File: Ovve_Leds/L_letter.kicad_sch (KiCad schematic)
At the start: 0 parts

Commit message: Finished preliminary schematics
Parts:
- added D23, D24, D25, D26, D27, D28, D29: LED, symbol Device:LED
- added H19, H20, H21, H22: MountingHole, symbol Mechanical:MountingHole
- added R23, R24, R25, R26, R27, R28, R29: 150, symbol Device:R
- added U3: 74LS174, symbol 74xx:74LS174
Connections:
- net CLK_in_L: now also U3.9 (Cp)
- net DATA_in_L: now also U3.3 (D0)
- new net: D27.2 (A), R27.2
- new net: D28.2 (A), R28.2
- new net: D26.2 (A), R26.2
- new net: D29.2 (A), R29.2
- new net: D24.2 (A), R24.2
- new net: D25.2 (A), R25.2
- new net: D23.2 (A), R23.2
- new net +5V: U3.1 (~{Mr}), U3.16 (VCC)
- new net GND: D23.1 (K), D24.1 (K), D25.1 (K), D26.1 (K), D27.1 (K), D28.1 (K), D29.1 (K), U3.8 (GND)
- new net LED1: R23.1, U3.2 (Q0), U3.4 (D1)
- new net LED2: R24.1, U3.5 (Q1), U3.6 (D2)
- new net LED3: R25.1, U3.11 (D3), U3.7 (Q2)
- new net LED4: R26.1, U3.10 (Q3), U3.13 (D4)
- new net LED5: R27.1, R28.1, R29.1, U3.12 (Q4)
- no-connect marks 0 -> 2

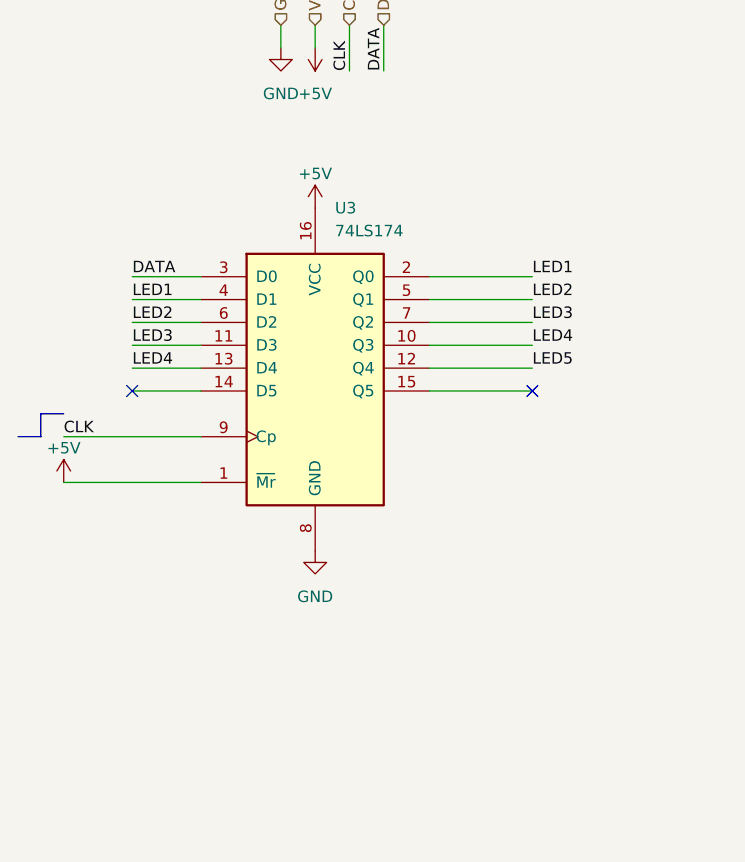
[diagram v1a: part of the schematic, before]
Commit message: Added decoupling capacitors and assigned footprints
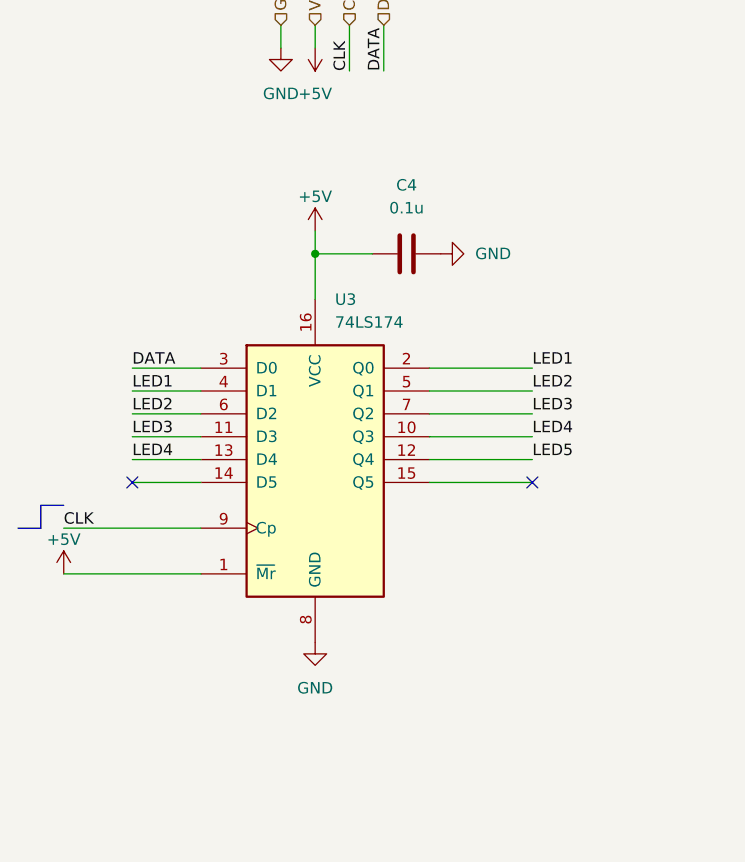
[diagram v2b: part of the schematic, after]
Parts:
- added C4: 0.1u, Capacitor_SMD:C_0603_1608Metric, symbol Device:C
- D23, D24, D25, D26, D27, D28, D29: footprint (none) -> LED_THT:LED_D5.0mm
- H19, H20, H21, H22: footprint (none) -> MountingHole:MountingHole_5.3mm_M5_DIN965_Pad
- R23, R24, R25, R26, R27, R28, R29: footprint (none) -> Resistor_SMD:R_0603_1608Metric
- U3: footprint (none) -> Package_DIP:DIP-16_W7.62mm
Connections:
- net +5V: now also C4.1
- net GND: now also C4.2
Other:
- moved on the sheet: U3

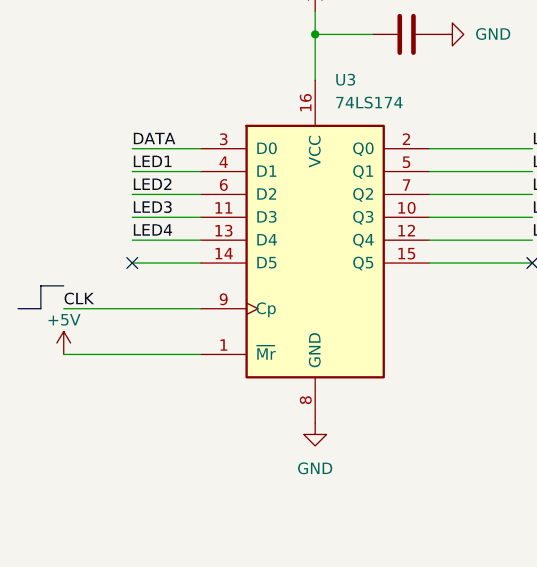
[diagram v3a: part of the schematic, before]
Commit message: Updated flip-flops
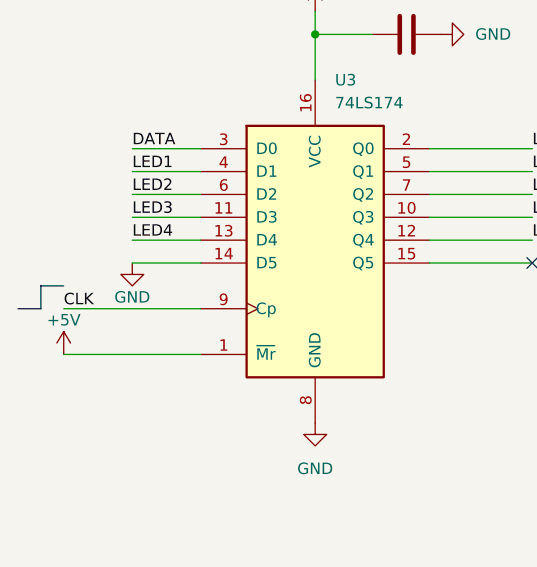
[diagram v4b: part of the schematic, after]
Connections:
- net GND: now also U3.14 (D5)
- no-connect marks 2 -> 1
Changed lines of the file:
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@@
 		(at 74.93 82.55)
-	)
-	(no_connect
-		(at 30.48 82.55)
 	)
 	(wire
@@
 					(unit 1)
 				)
+			)
+		)
+	)
+	(symbol
+		(lib_id "power:GND")
+		(at 30.48 82.55 0)
+		(unit 1)
+		(exclude_from_sim no)
+		(in_bom yes)
+		(on_board yes)
+		(dnp no)
+		(property "Reference" "#PWR074"
+			(at 30.48 88.9 0)
+			(effects
+				(font
+					(size 1.27 1.27)
+				)
+				(hide yes)
+			)
+		)
+		(property "Value" "GND"
+			(at 30.48 86.36 0)
+			(effects
+				(font
+					(size 1.27 1.27)
+				)
+			)
+		)
+		(property "Footprint" ""
+			(at 30.48 82.55 0)
+			(effects
+				(font
+					(size 1.27 1.27)
+				)
+				(hide yes)
+			)
+		)
+		(property "Datasheet" ""
+			(at 30.48 82.55 0)
+			(effects
+				(font
+					(size 1.27 1.27)
+				)
+				(hide yes)
+			)
+		)
+		(property "Description" "Power symbol creates a global label with name \"GND\" , ground"
+			(at 30.48 82.55 0)
+			(effects
+				(font
+					(size 1.27 1.27)
+				)
+				(hide yes)
+			)
+		)
+		(pin "1"
+		)
+		(instances
+			(project "Ovve_Leds"
+				(path "/a3f154e4-ded7-4c3a-b779-1e1dc74aad12/74d7af5f-3f5b-4383-b213-68bb9c4ec1cd"
+					(reference "#PWR074")
+					(unit 1)
+				)

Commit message: Component layout on PCB
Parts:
- removed H21, H22: MountingHole, MountingHole:MountingHole_5.3mm_M5_DIN965_Pad, symbol Mechanical:MountingHole
- added H25, H26: MountingHole, MountingHole:MountingHole_5.3mm_M5_DIN965_Pad, symbol Mechanical:MountingHole
- renumbered H19 to H21, H20 to H22
